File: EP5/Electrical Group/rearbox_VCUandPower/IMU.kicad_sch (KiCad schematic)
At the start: 8 parts, among them J27 I2C

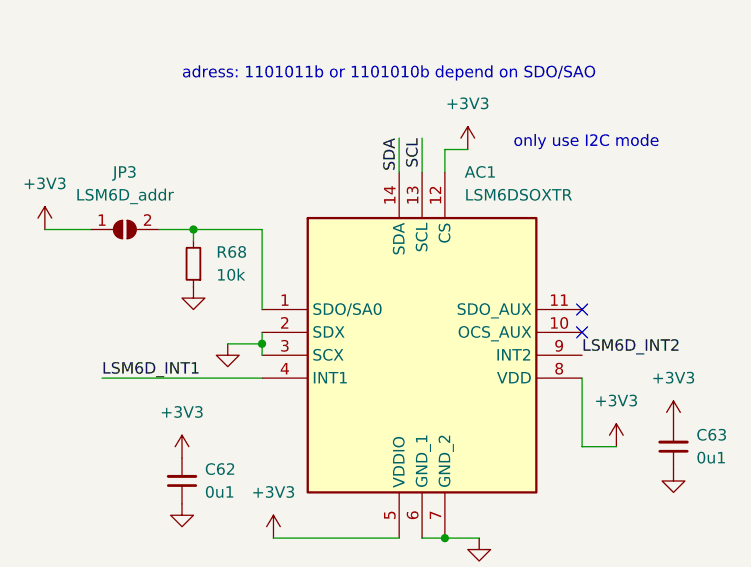
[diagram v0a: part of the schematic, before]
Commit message: add rearbox_VCUandPower to EP5
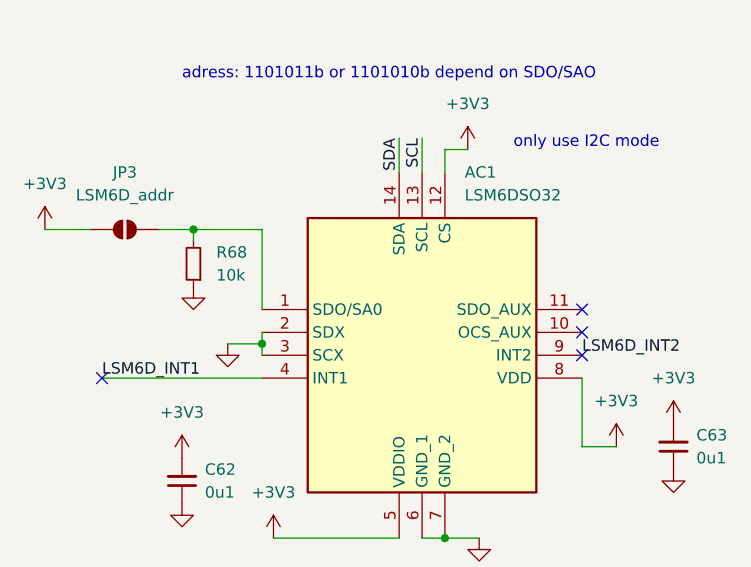
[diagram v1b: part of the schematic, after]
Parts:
- AC1: value LSM6DSOXTR -> LSM6DSO32
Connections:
- no-connect marks 2 -> 4
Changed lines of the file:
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@@
 		(rev "1.0")
 		(company "NTURacing")
-		(comment 1 "郭哲明")
+		(comment 1 "郭哲明 Jack Kuo")
 		(comment 2 "Electrical group")
 	)
@@
 	)
 	(no_connect
+		(at 106.68 123.19)
+	)
+	(no_connect
+		(at 53.34 125.73)
+	)
+	(no_connect
 		(at 106.68 120.65)
 	)
@@
 			)
 		)
-		(property "Description" ""
+		(property "Description" "Power symbol creates a global label with name \"+3V3\""
 			(at 46.99 109.22 0)
 			(effects
@@
 			)
 		)
-		(property "Description" ""
+		(property "Description" "Unpolarized capacitor, small symbol"
 			(at 62.23 137.16 0)
 			(effects
@@
 			)
 		)
-		(property "Description" ""
+		(property "Description" "Power symbol creates a global label with name \"+3V3\""
 			(at 93.98 100.33 0)
 			(effects
@@
 			)
 		)
-		(property "Description" ""
+		(property "Description" "Power symbol creates a global label with name \"GND\" , ground"
 			(at 67.31 121.92 0)
 			(effects
@@
 			)
 		)
-		(property "Description" ""
+		(property "Description" "Power symbol creates a global label with name \"+3V3\""
 			(at 72.39 143.51 0)
 			(effects
@@
 			)
 		)
-		(property "Description" ""
+		(property "Description" "Solder Jumper, 2-pole, open"
 			(at 55.88 109.22 0)
 			(effects
@@
 			)
 		)
-		(property "Description" ""
+		(property "Description" "Power symbol creates a global label with name \"+3V3\""
 			(at 204.47 102.87 0)
 			(effects
@@
 			)
 		)
-		(property "Description" ""
+		(property "Description" "Power symbol creates a global label with name \"+3V3\""
 			(at 116.84 130.81 0)
 			(effects
@@
 			)
 		)
-		(property "Value" "LSM6DSOXTR"
+		(property "Value" "LSM6DSO32"
 			(at 93.6341 105.41 0)
 			(effects
@@
 			)
 		)
-		(property "Description" ""
+		(property "Description" "IMUs - Inertial Measurement Units iNEMO inertial module: always-on 3D accelerometer and 3D gyroscope"
 			(at 71.12 118.11 0)
 			(effects
@@
 			)
 		)
-		(property "Description" ""
+		(property "Description" "Resistor, small symbol"
 			(at 63.5 113.03 0)
 			(effects
@@
 			)
 		)
-		(property "Description" ""
+		(property "Description" "Power symbol creates a global label with name \"+3V3\""
 			(at 62.23 134.62 0)
 			(effects
@@
 			)
 		)
-		(property "Description" ""
+		(property "Description" "Resistor, small symbol"
 			(at 207.01 118.11 0)
 			(effects
@@
 			)
 		)
-		(property "Description" ""
+		(property "Description" "Power symbol creates a global label with name \"GND\" , ground"
 			(at 63.5 115.57 0)
 			(effects
@@
 			)
 		)
-		(property "Description" ""
+		(property "Description" "Unpolarized capacitor, small symbol"
 			(at 116.84 133.35 0)
 			(effects
@@
 			)
 		)
-		(property "Description" ""
+		(property "Description" "Power symbol creates a global label with name \"+3V3\""
 			(at 110.49 133.35 0)
 			(effects
@@
 			)
 		)
-		(property "Description" ""
+		(property "Description" "Generic connector, single row, 01x02, script generated (kicad-library-utils/schlib/autogen/connector/)"
 			(at 228.6 110.49 0)
 			(effects
@@
 			)
 		)
-		(property "Description" ""
+		(property "Description" "Power symbol creates a global label with name \"GND\" , ground"
 			(at 95.25 143.51 0)
 			(effects
@@
 			)
 		)
-		(property "Description" ""
+		(property "Description" "Resistor, small symbol"
 			(at 207.01 107.95 0)
 			(effects
@@
 			)
 		)
-		(property "Description" ""
+		(property "Description" "Power symbol creates a global label with name \"GND\" , ground"
 			(at 62.23 139.7 0)
 			(effects
@@
 			)
 		)
-		(property "Description" ""
+		(property "Description" "Power symbol creates a global label with name \"GND\" , ground"
 			(at 116.84 135.89 0)
 			(effects
